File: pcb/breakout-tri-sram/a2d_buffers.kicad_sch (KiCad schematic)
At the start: 48 parts, among them U201 74LCX541FT, U202 74LCX541FT, U203 74LCX541FT, U204 74LCX541FT, U205 74LCX541FT, U206 74LCX541FT, U207 74LCX541FT, U208 74LCX541FT, U209 74LCX541FT, U210 74LCX541FT, U211 74LCX541FT, U212 74LCX541FT

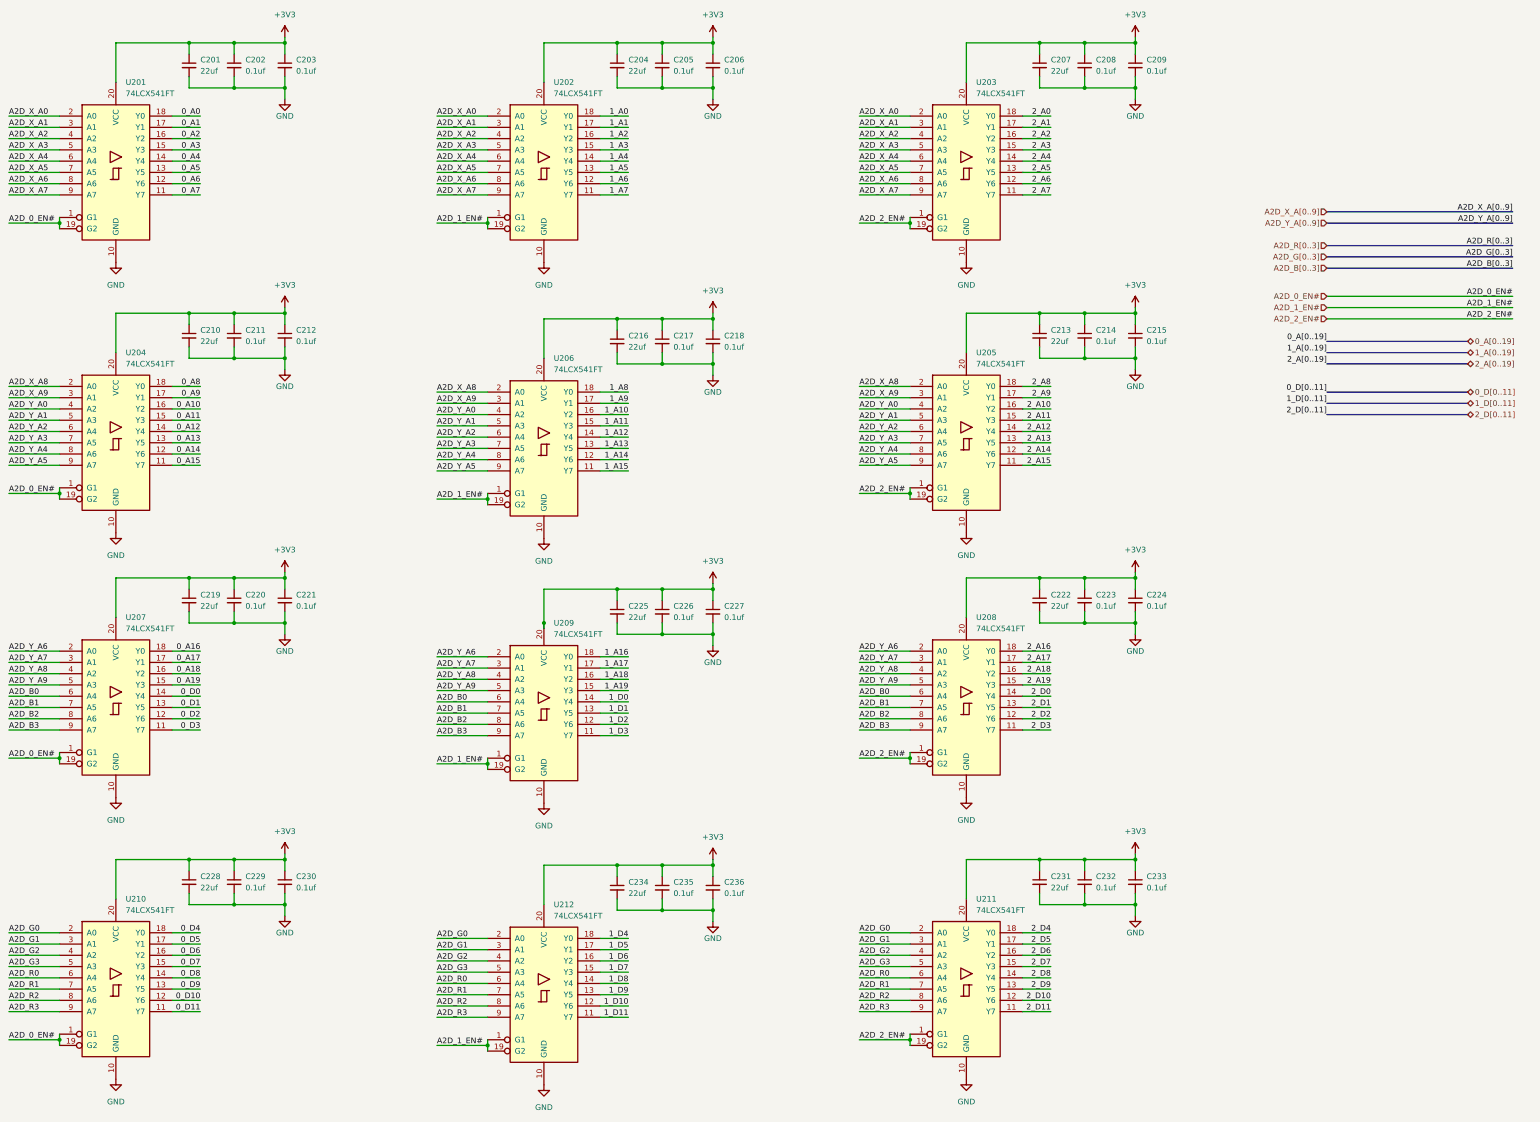
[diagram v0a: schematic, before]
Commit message: [pci][pci-sram] move to latched buffers
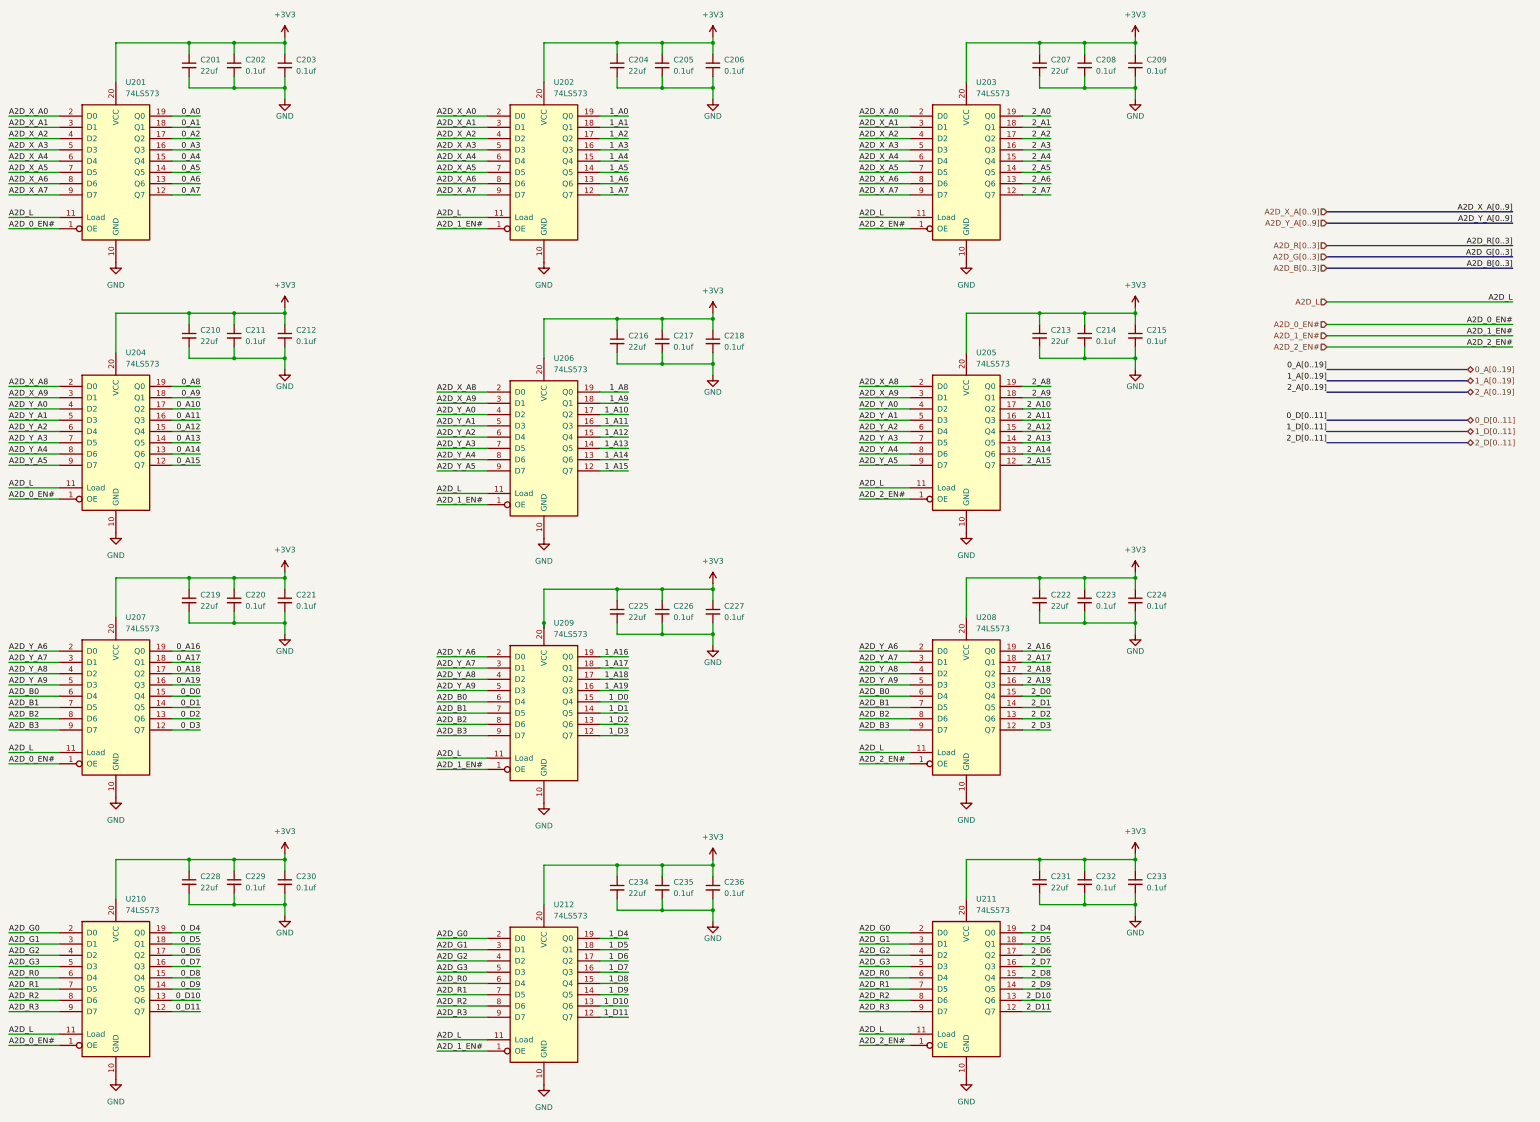
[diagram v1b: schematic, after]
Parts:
- U201, U202, U203, U204, U205, U206, U207, U208, U209, U210, U211, U212: value 74LCX541FT -> 74LS573; symbol 74xx:74LS541 -> 74xx:74LS573
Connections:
- net 0_A0: now also U201.19 (Q0); no longer U201.18 (Y0)
- net 0_A1: now also U201.18 (Q1); no longer U201.17 (Y1)
- net 0_A10: now also U204.17 (Q2); no longer U204.16 (Y2)
- net 0_A11: now also U204.16 (Q3); no longer U204.15 (Y3)
- net 0_A12: now also U204.15 (Q4); no longer U204.14 (Y4)
- net 0_A13: now also U204.14 (Q5); no longer U204.13 (Y5)
- net 0_A14: now also U204.13 (Q6); no longer U204.12 (Y6)
- net 0_A15: now also U204.12 (Q7); no longer U204.11 (Y7)
- net 0_A16: now also U207.19 (Q0); no longer U207.18 (Y0)
- net 0_A17: now also U207.18 (Q1); no longer U207.17 (Y1)
- net 0_A18: now also U207.17 (Q2); no longer U207.16 (Y2)
- net 0_A19: now also U207.16 (Q3); no longer U207.15 (Y3)
- net 0_A2: now also U201.17 (Q2); no longer U201.16 (Y2)
- net 0_A3: now also U201.16 (Q3); no longer U201.15 (Y3)
- net 0_A4: now also U201.15 (Q4); no longer U201.14 (Y4)
- net 0_A5: now also U201.14 (Q5); no longer U201.13 (Y5)
- net 0_A6: now also U201.13 (Q6); no longer U201.12 (Y6)
- net 0_A7: now also U201.12 (Q7); no longer U201.11 (Y7)
- net 0_A8: now also U204.19 (Q0); no longer U204.18 (Y0)
- net 0_A9: now also U204.18 (Q1); no longer U204.17 (Y1)
- net 0_D0: now also U207.15 (Q4); no longer U207.14 (Y4)
- net 0_D1: now also U207.14 (Q5); no longer U207.13 (Y5)
- net 0_D10: now also U210.13 (Q6); no longer U210.12 (Y6)
- net 0_D11: now also U210.12 (Q7); no longer U210.11 (Y7)
- net 0_D2: now also U207.13 (Q6); no longer U207.12 (Y6)
- net 0_D3: now also U207.12 (Q7); no longer U207.11 (Y7)
- net 0_D4: now also U210.19 (Q0); no longer U210.18 (Y0)
- net 0_D5: now also U210.18 (Q1); no longer U210.17 (Y1)
- net 0_D6: now also U210.17 (Q2); no longer U210.16 (Y2)
- net 0_D7: now also U210.16 (Q3); no longer U210.15 (Y3)
- net 0_D8: now also U210.15 (Q4); no longer U210.14 (Y4)
- net 0_D9: now also U210.14 (Q5); no longer U210.13 (Y5)
- net 1_A0: now also U202.19 (Q0); no longer U202.18 (Y0)
- net 1_A1: now also U202.18 (Q1); no longer U202.17 (Y1)
- net 1_A10: now also U206.17 (Q2); no longer U206.16 (Y2)
- net 1_A11: now also U206.16 (Q3); no longer U206.15 (Y3)
- net 1_A12: now also U206.15 (Q4); no longer U206.14 (Y4)
- net 1_A13: now also U206.14 (Q5); no longer U206.13 (Y5)
- net 1_A14: now also U206.13 (Q6); no longer U206.12 (Y6)
- net 1_A15: now also U206.12 (Q7); no longer U206.11 (Y7)
- net 1_A16: now also U209.19 (Q0); no longer U209.18 (Y0)
- net 1_A17: now also U209.18 (Q1); no longer U209.17 (Y1)
- net 1_A18: now also U209.17 (Q2); no longer U209.16 (Y2)
- net 1_A19: now also U209.16 (Q3); no longer U209.15 (Y3)
- net 1_A2: now also U202.17 (Q2); no longer U202.16 (Y2)
- net 1_A3: now also U202.16 (Q3); no longer U202.15 (Y3)
- net 1_A4: now also U202.15 (Q4); no longer U202.14 (Y4)
- net 1_A5: now also U202.14 (Q5); no longer U202.13 (Y5)
- net 1_A6: now also U202.13 (Q6); no longer U202.12 (Y6)
- net 1_A7: now also U202.12 (Q7); no longer U202.11 (Y7)
- net 1_A8: now also U206.19 (Q0); no longer U206.18 (Y0)
- net 1_A9: now also U206.18 (Q1); no longer U206.17 (Y1)
- net 1_D0: now also U209.15 (Q4); no longer U209.14 (Y4)
- net 1_D1: now also U209.14 (Q5); no longer U209.13 (Y5)
- net 1_D10: now also U212.13 (Q6); no longer U212.12 (Y6)
- net 1_D11: now also U212.12 (Q7); no longer U212.11 (Y7)
- net 1_D2: now also U209.13 (Q6); no longer U209.12 (Y6)
- net 1_D3: now also U209.12 (Q7); no longer U209.11 (Y7)
- net 1_D4: now also U212.19 (Q0); no longer U212.18 (Y0)
- net 1_D5: now also U212.18 (Q1); no longer U212.17 (Y1)
- net 1_D6: now also U212.17 (Q2); no longer U212.16 (Y2)
- net 1_D7: now also U212.16 (Q3); no longer U212.15 (Y3)
- net 1_D8: now also U212.15 (Q4); no longer U212.14 (Y4)
- net 1_D9: now also U212.14 (Q5); no longer U212.13 (Y5)
- net 2_A0: now also U203.19 (Q0); no longer U203.18 (Y0)
- net 2_A1: now also U203.18 (Q1); no longer U203.17 (Y1)
- net 2_A10: now also U205.17 (Q2); no longer U205.16 (Y2)
- net 2_A11: now also U205.16 (Q3); no longer U205.15 (Y3)
- net 2_A12: now also U205.15 (Q4); no longer U205.14 (Y4)
- net 2_A13: now also U205.14 (Q5); no longer U205.13 (Y5)
- net 2_A14: now also U205.13 (Q6); no longer U205.12 (Y6)
- net 2_A15: now also U205.12 (Q7); no longer U205.11 (Y7)
- net 2_A16: now also U208.19 (Q0); no longer U208.18 (Y0)
- net 2_A17: now also U208.18 (Q1); no longer U208.17 (Y1)
- net 2_A18: now also U208.17 (Q2); no longer U208.16 (Y2)
- net 2_A19: now also U208.16 (Q3); no longer U208.15 (Y3)
- net 2_A2: now also U203.17 (Q2); no longer U203.16 (Y2)
- net 2_A3: now also U203.16 (Q3); no longer U203.15 (Y3)
- net 2_A4: now also U203.15 (Q4); no longer U203.14 (Y4)
- net 2_A5: now also U203.14 (Q5); no longer U203.13 (Y5)
- net 2_A6: now also U203.13 (Q6); no longer U203.12 (Y6)
- net 2_A7: now also U203.12 (Q7); no longer U203.11 (Y7)
- net 2_A8: now also U205.19 (Q0); no longer U205.18 (Y0)
- net 2_A9: now also U205.18 (Q1); no longer U205.17 (Y1)
- net 2_D0: now also U208.15 (Q4); no longer U208.14 (Y4)
- net 2_D1: now also U208.14 (Q5); no longer U208.13 (Y5)
- net 2_D10: now also U211.13 (Q6); no longer U211.12 (Y6)
- net 2_D11: now also U211.12 (Q7); no longer U211.11 (Y7)
- net 2_D2: now also U208.13 (Q6); no longer U208.12 (Y6)
- net 2_D3: now also U208.12 (Q7); no longer U208.11 (Y7)
- net 2_D4: now also U211.19 (Q0); no longer U211.18 (Y0)
- net 2_D5: now also U211.18 (Q1); no longer U211.17 (Y1)
- net 2_D6: now also U211.17 (Q2); no longer U211.16 (Y2)
- net 2_D7: now also U211.16 (Q3); no longer U211.15 (Y3)
- net 2_D8: now also U211.15 (Q4); no longer U211.14 (Y4)
- net 2_D9: now also U211.14 (Q5); no longer U211.13 (Y5)
- net A2D_0_EN#: no longer U201.19 (G2), U204.19 (G2), U207.19 (G2), U210.19 (G2)
- net A2D_1_EN#: no longer U202.19 (G2), U206.19 (G2), U209.19 (G2), U212.19 (G2)
- net A2D_2_EN#: no longer U203.19 (G2), U205.19 (G2), U208.19 (G2), U211.19 (G2)
- new net A2D_L: U201.11 (Load), U202.11 (Load), U203.11 (Load), U204.11 (Load), U205.11 (Load), U206.11 (Load), U207.11 (Load), U208.11 (Load), U209.11 (Load), U210.11 (Load), U211.11 (Load), U212.11 (Load)

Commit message: [pcb][tri-sram] 3xsram routed
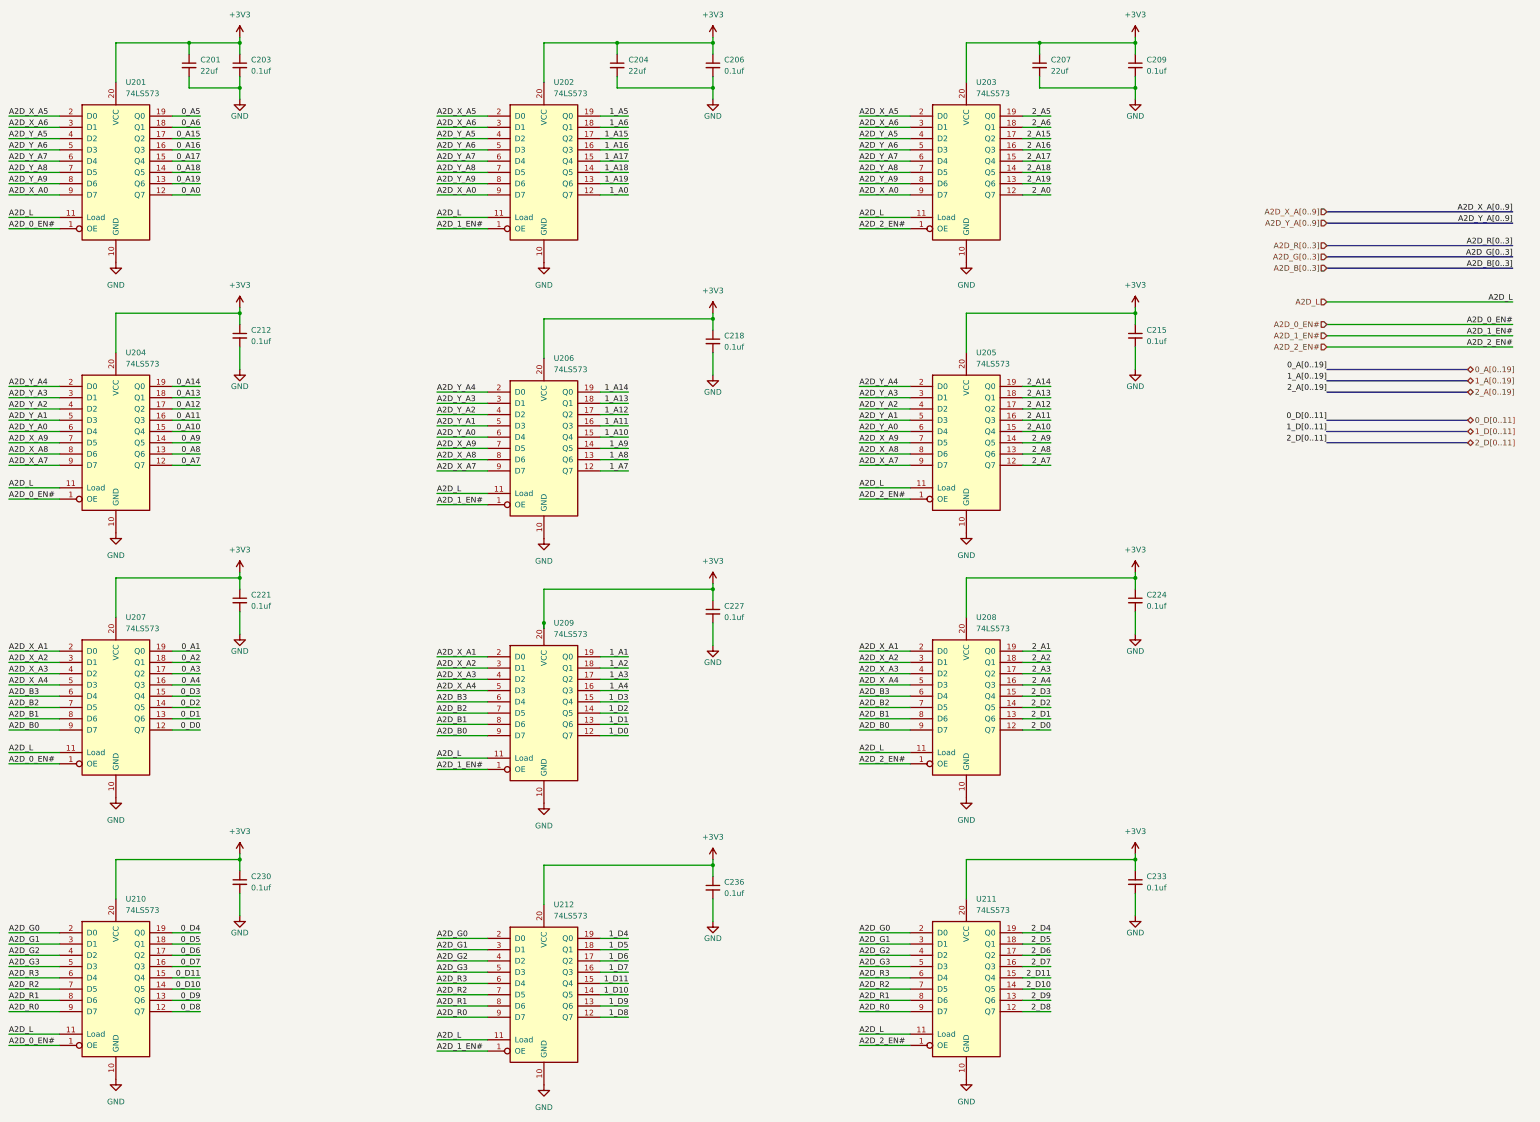
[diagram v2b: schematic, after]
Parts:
- removed C202, C205, C208, C211, C214, C217, C220, C223, C226, C229, C232, C235: 0.1uf, Capacitor_SMD:C_0402_1005Metric, symbol Device:C_Small
- removed C210, C213, C216, C219, C222, C225, C228, C231, C234: 22uf, Capacitor_SMD:C_0603_1608Metric, symbol Device:C_Small
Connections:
- net 0_A0: now also U201.12 (Q7); no longer U201.19 (Q0)
- net 0_A1: now also U207.19 (Q0); no longer U201.18 (Q1)
- net 0_A10: now also U204.15 (Q4); no longer U204.17 (Q2)
- net 0_A12: now also U204.17 (Q2); no longer U204.15 (Q4)
- net 0_A13: now also U204.18 (Q1); no longer U204.14 (Q5)
- net 0_A14: now also U204.19 (Q0); no longer U204.13 (Q6)
- net 0_A15: now also U201.17 (Q2); no longer U204.12 (Q7)
- net 0_A16: now also U201.16 (Q3); no longer U207.19 (Q0)
- net 0_A17: now also U201.15 (Q4); no longer U207.18 (Q1)
- net 0_A18: now also U201.14 (Q5); no longer U207.17 (Q2)
- net 0_A19: now also U201.13 (Q6); no longer U207.16 (Q3)
- net 0_A2: now also U207.18 (Q1); no longer U201.17 (Q2)
- net 0_A3: now also U207.17 (Q2); no longer U201.16 (Q3)
- net 0_A4: now also U207.16 (Q3); no longer U201.15 (Q4)
- net 0_A5: now also U201.19 (Q0); no longer U201.14 (Q5)
- net 0_A6: now also U201.18 (Q1); no longer U201.13 (Q6)
- net 0_A7: now also U204.12 (Q7); no longer U201.12 (Q7)
- net 0_A8: now also U204.13 (Q6); no longer U204.19 (Q0)
- net 0_A9: now also U204.14 (Q5); no longer U204.18 (Q1)
- net 0_D0: now also U207.12 (Q7); no longer U207.15 (Q4)
- net 0_D1: now also U207.13 (Q6); no longer U207.14 (Q5)
- net 0_D10: now also U210.14 (Q5); no longer U210.13 (Q6)
- net 0_D11: now also U210.15 (Q4); no longer U210.12 (Q7)
- net 0_D2: now also U207.14 (Q5); no longer U207.13 (Q6)
- net 0_D3: now also U207.15 (Q4); no longer U207.12 (Q7)
- net 0_D8: now also U210.12 (Q7); no longer U210.15 (Q4)
- net 0_D9: now also U210.13 (Q6); no longer U210.14 (Q5)
- net 1_A0: now also U202.12 (Q7); no longer U202.19 (Q0)
- net 1_A1: now also U209.19 (Q0); no longer U202.18 (Q1)
- net 1_A10: now also U206.15 (Q4); no longer U206.17 (Q2)
- net 1_A12: now also U206.17 (Q2); no longer U206.15 (Q4)
- net 1_A13: now also U206.18 (Q1); no longer U206.14 (Q5)
- net 1_A14: now also U206.19 (Q0); no longer U206.13 (Q6)
- net 1_A15: now also U202.17 (Q2); no longer U206.12 (Q7)
- net 1_A16: now also U202.16 (Q3); no longer U209.19 (Q0)
- net 1_A17: now also U202.15 (Q4); no longer U209.18 (Q1)
- net 1_A18: now also U202.14 (Q5); no longer U209.17 (Q2)
- net 1_A19: now also U202.13 (Q6); no longer U209.16 (Q3)
- net 1_A2: now also U209.18 (Q1); no longer U202.17 (Q2)
- net 1_A3: now also U209.17 (Q2); no longer U202.16 (Q3)
- net 1_A4: now also U209.16 (Q3); no longer U202.15 (Q4)
- net 1_A5: now also U202.19 (Q0); no longer U202.14 (Q5)
- net 1_A6: now also U202.18 (Q1); no longer U202.13 (Q6)
- net 1_A7: now also U206.12 (Q7); no longer U202.12 (Q7)
- net 1_A8: now also U206.13 (Q6); no longer U206.19 (Q0)
- net 1_A9: now also U206.14 (Q5); no longer U206.18 (Q1)
- net 1_D0: now also U209.12 (Q7); no longer U209.15 (Q4)
- net 1_D1: now also U209.13 (Q6); no longer U209.14 (Q5)
- net 1_D10: now also U212.14 (Q5); no longer U212.13 (Q6)
- net 1_D11: now also U212.15 (Q4); no longer U212.12 (Q7)
- net 1_D2: now also U209.14 (Q5); no longer U209.13 (Q6)
- net 1_D3: now also U209.15 (Q4); no longer U209.12 (Q7)
- net 1_D8: now also U212.12 (Q7); no longer U212.15 (Q4)
- net 1_D9: now also U212.13 (Q6); no longer U212.14 (Q5)
- net 2_A0: now also U203.12 (Q7); no longer U203.19 (Q0)
- net 2_A1: now also U208.19 (Q0); no longer U203.18 (Q1)
- net 2_A10: now also U205.15 (Q4); no longer U205.17 (Q2)
- net 2_A12: now also U205.17 (Q2); no longer U205.15 (Q4)
- net 2_A13: now also U205.18 (Q1); no longer U205.14 (Q5)
- net 2_A14: now also U205.19 (Q0); no longer U205.13 (Q6)
- net 2_A15: now also U203.17 (Q2); no longer U205.12 (Q7)
- net 2_A16: now also U203.16 (Q3); no longer U208.19 (Q0)
- net 2_A17: now also U203.15 (Q4); no longer U208.18 (Q1)
- net 2_A18: now also U203.14 (Q5); no longer U208.17 (Q2)
- net 2_A19: now also U203.13 (Q6); no longer U208.16 (Q3)
- net 2_A2: now also U208.18 (Q1); no longer U203.17 (Q2)
- net 2_A3: now also U208.17 (Q2); no longer U203.16 (Q3)
- net 2_A4: now also U208.16 (Q3); no longer U203.15 (Q4)
- net 2_A5: now also U203.19 (Q0); no longer U203.14 (Q5)
- net 2_A6: now also U203.18 (Q1); no longer U203.13 (Q6)
- net 2_A7: now also U205.12 (Q7); no longer U203.12 (Q7)
- net 2_A8: now also U205.13 (Q6); no longer U205.19 (Q0)
- net 2_A9: now also U205.14 (Q5); no longer U205.18 (Q1)
- net 2_D0: now also U208.12 (Q7); no longer U208.15 (Q4)
- net 2_D1: now also U208.13 (Q6); no longer U208.14 (Q5)
- net 2_D10: now also U211.14 (Q5); no longer U211.13 (Q6)
- net 2_D11: now also U211.15 (Q4); no longer U211.12 (Q7)
- net 2_D2: now also U208.14 (Q5); no longer U208.13 (Q6)
- net 2_D3: now also U208.15 (Q4); no longer U208.12 (Q7)
- net 2_D8: now also U211.12 (Q7); no longer U211.15 (Q4)
- net 2_D9: now also U211.13 (Q6); no longer U211.14 (Q5)
- net A2D_B0: now also U207.9 (D7), U208.9 (D7), U209.9 (D7); no longer U207.6 (D4), U208.6 (D4), U209.6 (D4)
- net A2D_B1: now also U207.8 (D6), U208.8 (D6), U209.8 (D6); no longer U207.7 (D5), U208.7 (D5), U209.7 (D5)
- net A2D_B2: now also U207.7 (D5), U208.7 (D5), U209.7 (D5); no longer U207.8 (D6), U208.8 (D6), U209.8 (D6)
- net A2D_B3: now also U207.6 (D4), U208.6 (D4), U209.6 (D4); no longer U207.9 (D7), U208.9 (D7), U209.9 (D7)
- net A2D_R0: now also U210.9 (D7), U211.9 (D7), U212.9 (D7); no longer U210.6 (D4), U211.6 (D4), U212.6 (D4)
- net A2D_R1: now also U210.8 (D6), U211.8 (D6), U212.8 (D6); no longer U210.7 (D5), U211.7 (D5), U212.7 (D5)
- net A2D_R2: now also U210.7 (D5), U211.7 (D5), U212.7 (D5); no longer U210.8 (D6), U211.8 (D6), U212.8 (D6)
- net A2D_R3: now also U210.6 (D4), U211.6 (D4), U212.6 (D4); no longer U210.9 (D7), U211.9 (D7), U212.9 (D7)
- net A2D_X_A0: now also U201.9 (D7), U202.9 (D7), U203.9 (D7); no longer U201.2 (D0), U202.2 (D0), U203.2 (D0)
- net A2D_X_A1: now also U207.2 (D0), U208.2 (D0), U209.2 (D0); no longer U201.3 (D1), U202.3 (D1), U203.3 (D1)
- net A2D_X_A2: now also U207.3 (D1), U208.3 (D1), U209.3 (D1); no longer U201.4 (D2), U202.4 (D2), U203.4 (D2)
- net A2D_X_A3: now also U207.4 (D2), U208.4 (D2), U209.4 (D2); no longer U201.5 (D3), U202.5 (D3), U203.5 (D3)
- net A2D_X_A4: now also U207.5 (D3), U208.5 (D3), U209.5 (D3); no longer U201.6 (D4), U202.6 (D4), U203.6 (D4)
- net A2D_X_A5: now also U201.2 (D0), U202.2 (D0), U203.2 (D0); no longer U201.7 (D5), U202.7 (D5), U203.7 (D5)
- net A2D_X_A6: now also U201.3 (D1), U202.3 (D1), U203.3 (D1); no longer U201.8 (D6), U202.8 (D6), U203.8 (D6)
- net A2D_X_A7: now also U204.9 (D7), U205.9 (D7), U206.9 (D7); no longer U201.9 (D7), U202.9 (D7), U203.9 (D7)
- net A2D_X_A8: now also U204.8 (D6), U205.8 (D6), U206.8 (D6); no longer U204.2 (D0), U205.2 (D0), U206.2 (D0)
- net A2D_X_A9: now also U204.7 (D5), U205.7 (D5), U206.7 (D5); no longer U204.3 (D1), U205.3 (D1), U206.3 (D1)
- net A2D_Y_A0: now also U204.6 (D4), U205.6 (D4), U206.6 (D4); no longer U204.4 (D2), U205.4 (D2), U206.4 (D2)
- net A2D_Y_A2: now also U204.4 (D2), U205.4 (D2), U206.4 (D2); no longer U204.6 (D4), U205.6 (D4), U206.6 (D4)
- net A2D_Y_A3: now also U204.3 (D1), U205.3 (D1), U206.3 (D1); no longer U204.7 (D5), U205.7 (D5), U206.7 (D5)
- net A2D_Y_A4: now also U204.2 (D0), U205.2 (D0), U206.2 (D0); no longer U204.8 (D6), U205.8 (D6), U206.8 (D6)
- net A2D_Y_A5: now also U201.4 (D2), U202.4 (D2), U203.4 (D2); no longer U204.9 (D7), U205.9 (D7), U206.9 (D7)
- net A2D_Y_A6: now also U201.5 (D3), U202.5 (D3), U203.5 (D3); no longer U207.2 (D0), U208.2 (D0), U209.2 (D0)
- net A2D_Y_A7: now also U201.6 (D4), U202.6 (D4), U203.6 (D4); no longer U207.3 (D1), U208.3 (D1), U209.3 (D1)
- net A2D_Y_A8: now also U201.7 (D5), U202.7 (D5), U203.7 (D5); no longer U207.4 (D2), U208.4 (D2), U209.4 (D2)
- net A2D_Y_A9: now also U201.8 (D6), U202.8 (D6), U203.8 (D6); no longer U207.5 (D3), U208.5 (D3), U209.5 (D3)
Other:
- moved on the sheet: C203, C212, C221, C230
